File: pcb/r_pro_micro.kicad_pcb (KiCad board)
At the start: 2 copper layers, 31.3 x 32.5 mm, 27 parts, among them J1 Conn_01x12, J2 USB_A, J3 Conn_01x12, U1 MIC5219-2.5YM5, U2 ATmega32U4-MU, Y1 16MHz

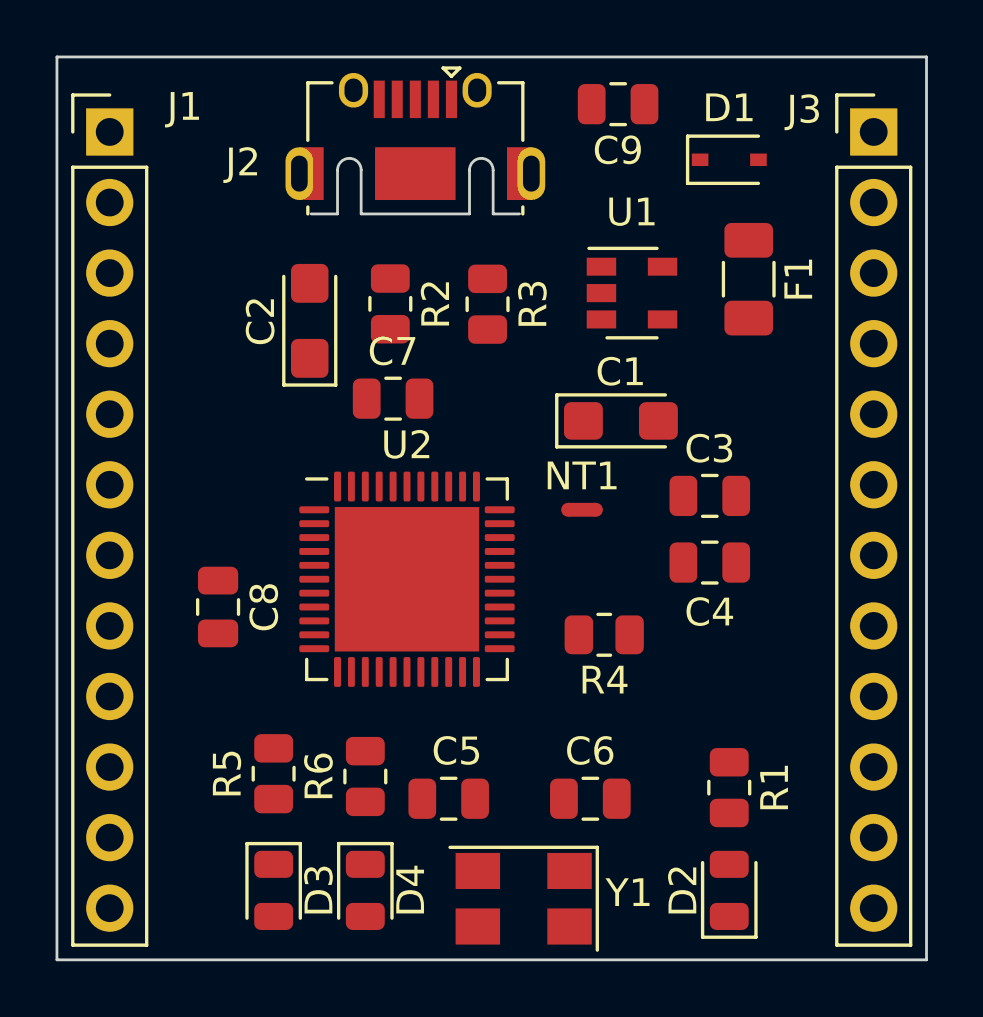
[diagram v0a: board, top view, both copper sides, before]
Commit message: ** Se corrige posicionamiento **
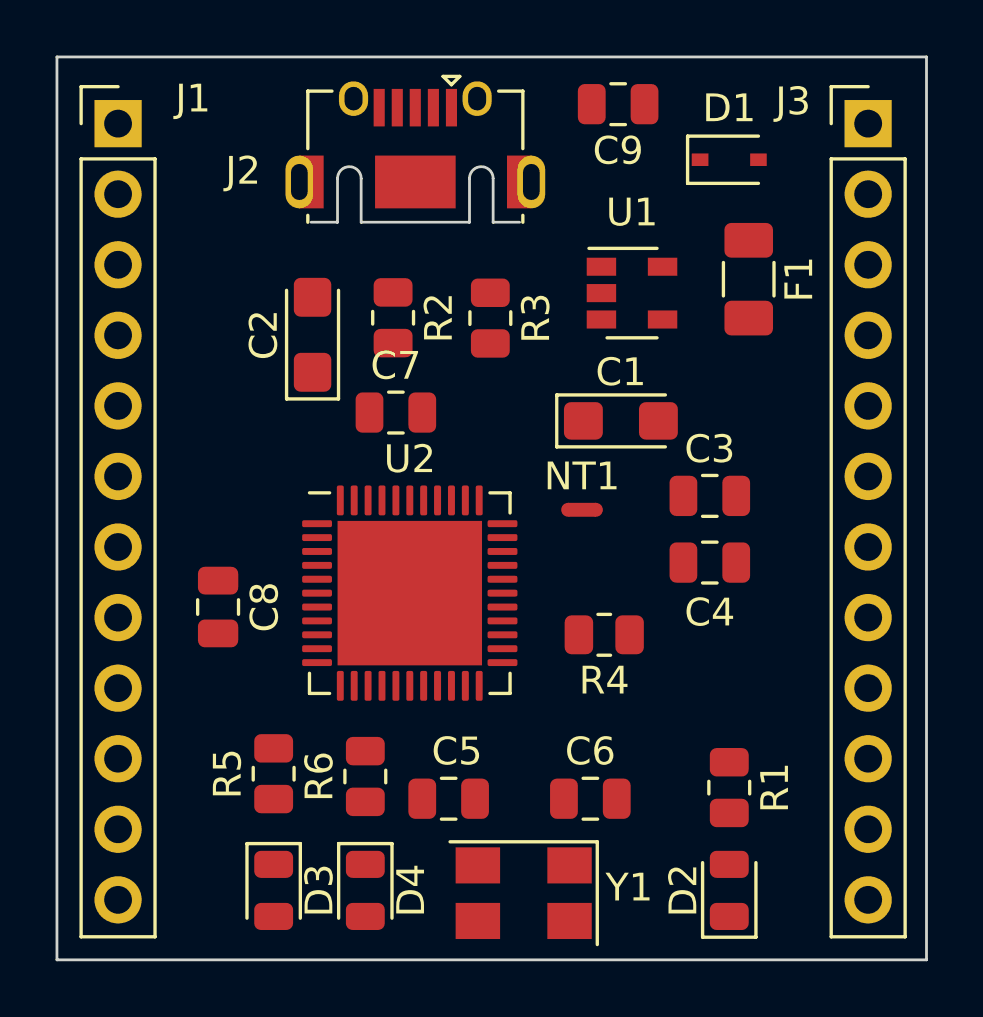
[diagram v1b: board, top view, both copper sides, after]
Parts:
- moved C2 0.51 mm to (145.0, 90.5)
- moved C7 0.51 mm to (148.0, 93.3)
- moved R2 0.51 mm to (147.9, 89.9)
- moved R3 0.51 mm to (151.4, 89.9)
- moved U2 0.51 mm to (148.5, 99.8)
- moved J1 0.42 mm to (138.0, 82.9)
- moved J3 0.36 mm to (165.0, 82.9)
- moved J2 0.30 mm to (148.7, 85.0)
- moved Y1 0.20 mm to (152.6, 110.6)
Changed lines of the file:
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@@
       (effects (font (size 1 1) (thickness 0.15)))
-    )
-    (fp_text user %R (at 0 0) (layer F.Fab)
-      (effects (font (size 0.8 0.8) (thickness 0.12)))
     )
     (fp_line (start 1.6 -0.8) (end -1.2 -0.8) (layer F.Fab) (width 0.1))
@@
     (fp_line (start 2.3 -1.05) (end 2.3 1.05) (layer F.CrtYd) (width 0.05))
     (fp_line (start 2.3 1.05) (end -2.3 1.05) (layer F.CrtYd) (width 0.05))
+    (fp_text user %R (at 0 0) (layer F.Fab)
+      (effects (font (size 0.8 0.8) (thickness 0.12)))
+    )
     (pad 2 smd roundrect (at 1.35 0) (size 1.4 1.35) (layers F.Cu F.Paste F.Mask) (roundrect_rratio 0.185185)
       (net 1 GND))
@@
   )
   (module Capacitor_Tantalum_SMD:CP_EIA-3216-10_Kemet-I (layer F.Cu)
-    (at 144.9 90 90)
+    (at 145 90.5 90)
     (descr "Tantalum Capacitor SMD Kemet-I (3216-10 Metric), IPC_7351 nominal, (Body size from: http://www.kemet.com/Lists/ProductCatalog/Attachments/253/KEM_TC101_STD.pdf), generated with kicad-footprint-generator")
     (tags "capacitor tantalum")
@@
       (effects (font (size 1 1) (thickness 0.15)))
     )
-    (fp_text user %R (at 0 0) (layer F.Fab)
-      (effects (font (size 0.5 0.5) (thickness 0.08)))
-    )
     (fp_line (start -1 0.625) (end -1 -0.625) (layer F.Fab) (width 0.1))
     (fp_line (start -1 -0.625) (end 1 -0.625) (layer F.Fab) (width 0.1))
@@
     (fp_line (start 1.7 -0.98) (end 1.7 0.98) (layer F.CrtYd) (width 0.05))
     (fp_line (start 1.7 0.98) (end -1.7 0.98) (layer F.CrtYd) (width 0.05))
+    (fp_text user %R (at 0 0) (layer F.Fab)
+      (effects (font (size 0.5 0.5) (thickness 0.08)))
+    )
     (pad 2 smd roundrect (at 0.95 0) (size 1 1.45) (layers F.Cu F.Paste F.Mask) (roundrect_rratio 0.25)
       (net 1 GND))
@@
       (effects (font (size 1 1) (thickness 0.15)))
     )
-    (fp_text user %R (at 0 0) (layer F.Fab)
-      (effects (font (size 0.5 0.5) (thickness 0.08)))
-    )
     (fp_line (start -1 0.625) (end -1 -0.625) (layer F.Fab) (width 0.1))
     (fp_line (start -1 -0.625) (end 1 -0.625) (layer F.Fab) (width 0.1))
@@
     (fp_line (start 1.7 -0.98) (end 1.7 0.98) (layer F.CrtYd) (width 0.05))
     (fp_line (start 1.7 0.98) (end -1.7 0.98) (layer F.CrtYd) (width 0.05))
+    (fp_text user %R (at 0 0) (layer F.Fab)
+      (effects (font (size 0.5 0.5) (thickness 0.08)))
+    )
     (pad 2 smd roundrect (at 0.95 0) (size 1 1.45) (layers F.Cu F.Paste F.Mask) (roundrect_rratio 0.25)
       (net 1 GND))
@@
   )
   (module Capacitor_SMD:C_0805_2012Metric (layer F.Cu)
-    (at 147.9 92.8)
+    (at 148 93.3)
     (descr "Capacitor SMD 0805 (2012 Metric), square (rectangular) end terminal, IPC_7351 nominal, (Body size source: IPC-SM-782 page 76, https://www.pcb-3d.com/wordpress/wp-content/uploads/ipc-sm-782a_amendment_1_and_2.pdf, https://docs.google.com/spreadsheets/d/1BsfQQcO9C6DZCsRaXUlFlo91Tg2WpOkGARC1WS5S8t0/edit?usp=sharing), generated with kicad-footprint-generator")
     (tags capacitor)
@@
       (effects (font (size 1 1) (thickness 0.15)))
     )
-    (fp_text user %R (at 0 0 90) (layer F.Fab)
-      (effects (font (size 0.5 0.5) (thickness 0.08)))
-    )
     (fp_line (start -1 0.625) (end -1 -0.625) (layer F.Fab) (width 0.1))
     (fp_line (start -1 -0.625) (end 1 -0.625) (layer F.Fab) (width 0.1))
@@
     (fp_line (start 1.7 -0.98) (end 1.7 0.98) (layer F.CrtYd) (width 0.05))
     (fp_line (start 1.7 0.98) (end -1.7 0.98) (layer F.CrtYd) (width 0.05))
+    (fp_text user %R (at 0 0 90) (layer F.Fab)
+      (effects (font (size 0.5 0.5) (thickness 0.08)))
+    )
     (pad 2 smd roundrect (at 0.95 0 270) (size 1 1.45) (layers F.Cu F.Paste F.Mask) (roundrect_rratio 0.25)
       (net 1 GND))
@@
       (effects (font (size 1 1) (thickness 0.15)))
     )
-    (fp_text user %R (at 0 0 90) (layer F.Fab)
-      (effects (font (size 0.5 0.5) (thickness 0.08)))
-    )
     (fp_line (start 1 -0.6) (end -0.7 -0.6) (layer F.Fab) (width 0.1))
     (fp_line (start -0.7 -0.6) (end -1 -0.3) (layer F.Fab) (width 0.1))
@@
     (fp_line (start 1.68 -0.95) (end 1.68 0.95) (layer F.CrtYd) (width 0.05))
     (fp_line (start 1.68 0.95) (end -1.68 0.95) (layer F.CrtYd) (width 0.05))
+    (fp_text user %R (at 0 0 90) (layer F.Fab)
+      (effects (font (size 0.5 0.5) (thickness 0.08)))
+    )
     (pad 2 smd roundrect (at 0.9375 0 270) (size 0.975 1.4) (layers F.Cu F.Paste F.Mask) (roundrect_rratio 0.25)
       (net 3 +3V3))
@@
   )
   (module Connector_PinHeader_2.54mm:PinHeader_1x12_P2.54mm_Vertical (layer F.Cu)
-    (at 137.7 83.2)
+    (at 138 82.9)
     (descr "Through hole straight pin header, 1x12, 2.54mm pitch, single row")
     (tags "Through hole pin header THT 1x12 2.54mm single row")
@@
     )
     (fp_text value Conn_01x12 (at 0 30.27) (layer F.Fab)
-      (effects (font (size 1 1) (thickness 0.15)))
-    )
-    (fp_text user %R (at 0 13.97 90) (layer F.Fab)
       (effects (font (size 1 1) (thickness 0.15)))
     )
@@
     (fp_line (start 1.8 29.75) (end 1.8 -1.8) (layer F.CrtYd) (width 0.05))
     (fp_line (start 1.8 -1.8) (end -1.8 -1.8) (layer F.CrtYd) (width 0.05))
+    (fp_text user %R (at 0 13.97 90) (layer F.Fab)
+      (effects (font (size 1 1) (thickness 0.15)))
+    )
     (pad 12 thru_hole oval (at 0 27.94) (size 1.7 1.7) (drill 1) (layers *.Cu *.Mask)
       (net 13 /TXO))
@@
   )
   (module Connector_USB:USB_Micro-AB_Molex_47590-0001 (layer F.Cu)
-    (at 148.7 84.7)
+    (at 148.7 85)
     (descr "Micro USB AB receptable, right-angle inverted (https://www.molex.com/pdm_docs/sd/475900001_sd.pdf)")
     (tags "Micro AB USB SMD")
@@
   )
   (module Connector_PinHeader_2.54mm:PinHeader_1x12_P2.54mm_Vertical (layer F.Cu)
-    (at 165.2 83.2)
+    (at 165 82.9)
     (descr "Through hole straight pin header, 1x12, 2.54mm pitch, single row")
     (tags "Through hole pin header THT 1x12 2.54mm single row")
-    (fp_text reference J3 (at -2.5 -0.8) (layer F.SilkS)
+    (fp_text reference J3 (at -2.7 -0.8) (layer F.SilkS)
       (effects (font (size 1 1) (thickness 0.15)))
     )
@@
   )
   (module Resistor_SMD:R_0805_2012Metric (layer F.Cu)
-    (at 147.8 89.3875 270)
+    (at 147.9 89.8875 270)
     (descr "Resistor SMD 0805 (2012 Metric), square (rectangular) end terminal, IPC_7351 nominal, (Body size source: IPC-SM-782 page 72, https://www.pcb-3d.com/wordpress/wp-content/uploads/ipc-sm-782a_amendment_1_and_2.pdf), generated with kicad-footprint-generator")
     (tags resistor)
@@
     (fp_text value 22 (at 0 1.65 90) (layer F.Fab)
       (effects (font (size 1 1) (thickness 0.15)))
-    )
-    (fp_text user %R (at 0 0 90) (layer F.Fab)
-      (effects (font (size 0.5 0.5) (thickness 0.08)))
     )
     (fp_line (start -1 0.625) (end -1 -0.625) (layer F.Fab) (width 0.1))
@@
     (fp_line (start 1.68 -0.95) (end 1.68 0.95) (layer F.CrtYd) (width 0.05))
     (fp_line (start 1.68 0.95) (end -1.68 0.95) (layer F.CrtYd) (width 0.05))
+    (fp_text user %R (at 0 0 90) (layer F.Fab)
+      (effects (font (size 0.5 0.5) (thickness 0.08)))
+    )
     (pad 2 smd roundrect (at 0.9125 0 270) (size 1.025 1.4) (layers F.Cu F.Paste F.Mask) (roundrect_rratio 0.243902)
       (net 24 "Net-(J2-Pad3)"))
@@
   )
   (module Resistor_SMD:R_0805_2012Metric (layer F.Cu)
-    (at 151.3 89.4 270)
+    (at 151.4 89.9 270)
     (descr "Resistor SMD 0805 (2012 Metric), square (rectangular) end terminal, IPC_7351 nominal, (Body size source: IPC-SM-782 page 72, https://www.pcb-3d.com/wordpress/wp-content/uploads/ipc-sm-782a_amendment_1_and_2.pdf), generated with kicad-footprint-generator")
     (tags resistor)
@@
       (effects (font (size 1 1) (thickness 0.15)))
     )
-    (fp_text user %R (at 0 0) (layer F.Fab)
-      (effects (font (size 0.5 0.5) (thickness 0.08)))
-    )
     (fp_line (start -1 0.625) (end -1 -0.625) (layer F.Fab) (width 0.1))
     (fp_line (start -1 -0.625) (end 1 -0.625) (layer F.Fab) (width 0.1))
@@
     (fp_line (start 1.68 -0.95) (end 1.68 0.95) (layer F.CrtYd) (width 0.05))
     (fp_line (start 1.68 0.95) (end -1.68 0.95) (layer F.CrtYd) (width 0.05))
+    (fp_text user %R (at 0 0) (layer F.Fab)
+      (effects (font (size 0.5 0.5) (thickness 0.08)))
+    )
     (pad 2 smd roundrect (at 0.9125 0 180) (size 1.025 1.4) (layers F.Cu F.Paste F.Mask) (roundrect_rratio 0.243902)
       (net 26 /RESET))
@@
       (effects (font (size 1 1) (thickness 0.15)))
     )
-    (fp_text user %R (at 0 0 90) (layer F.Fab)
-      (effects (font (size 0.5 0.5) (thickness 0.08)))
-    )
     (fp_line (start -1 0.625) (end -1 -0.625) (layer F.Fab) (width 0.1))
     (fp_line (start -1 -0.625) (end 1 -0.625) (layer F.Fab) (width 0.1))
@@
     (fp_line (start 1.68 -0.95) (end 1.68 0.95) (layer F.CrtYd) (width 0.05))
     (fp_line (start 1.68 0.95) (end -1.68 0.95) (layer F.CrtYd) (width 0.05))
+    (fp_text user %R (at 0 0 90) (layer F.Fab)
+      (effects (font (size 0.5 0.5) (thickness 0.08)))
+    )
     (pad 2 smd roundrect (at 0.9125 0 90) (size 1.025 1.4) (layers F.Cu F.Paste F.Mask) (roundrect_rratio 0.243902)
       (net 39 "Net-(R6-Pad2)"))
@@
   )
   (module Package_DFN_QFN:QFN-44-1EP_7x7mm_P0.5mm_EP5.2x5.2mm (layer F.Cu)
-    (at 148.4 99.3)
+    (at 148.5 99.8)
     (descr "QFN, 44 Pin (http://ww1.microchip.com/downloads/en/DeviceDoc/2512S.pdf#page=17), generated with kicad-footprint-generator ipc_noLead_generator.py")
     (tags "QFN NoLead")
@@
   )
   (module Crystal:Crystal_SMD_5032-4Pin_5.0x3.2mm (layer F.Cu)
-    (at 152.6 110.8 180)
+    (at 152.6 110.6 180)
     (descr "SMD Crystal SERIES SMD2520/4 http://www.icbase.com/File/PDF/HKC/HKC00061008.pdf, 5.0x3.2mm^2 package")
     (tags "SMD SMT crystal")

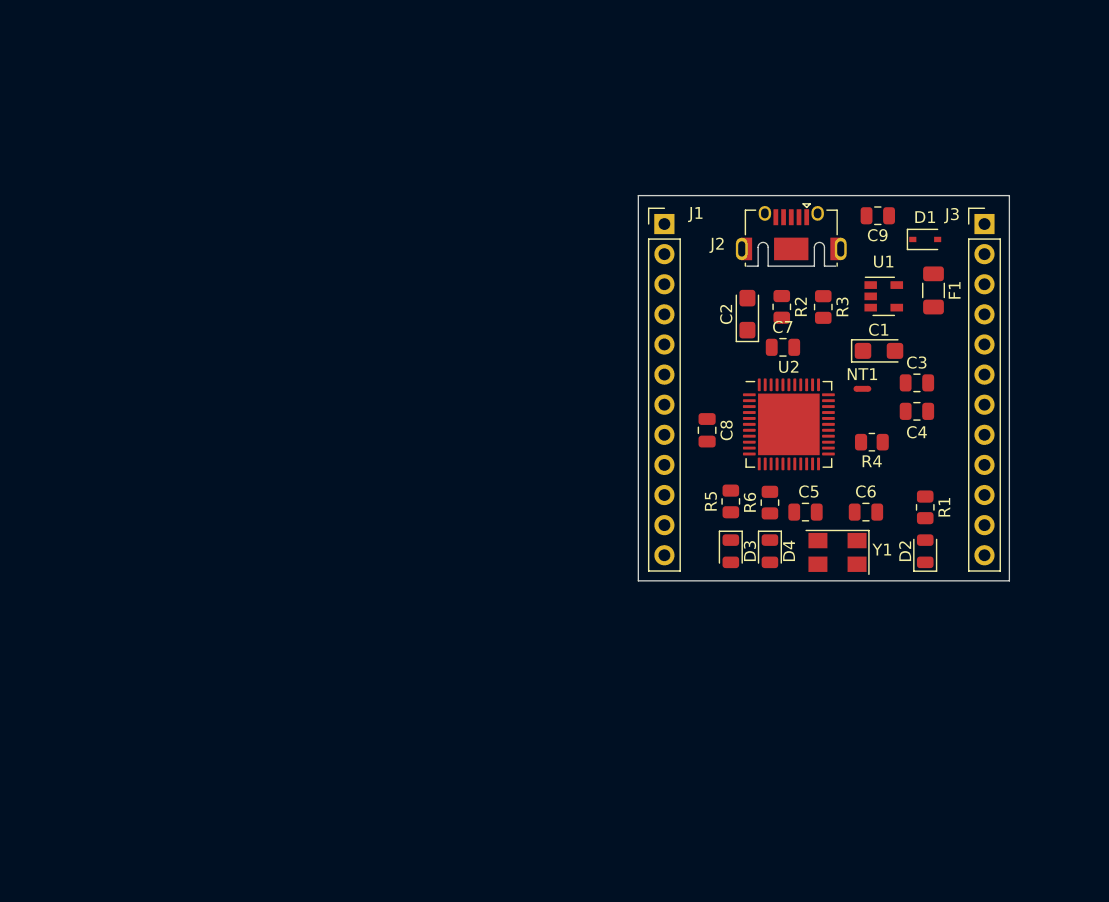
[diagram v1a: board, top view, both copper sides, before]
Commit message: ** Se rehace posicionamiento de footprints **
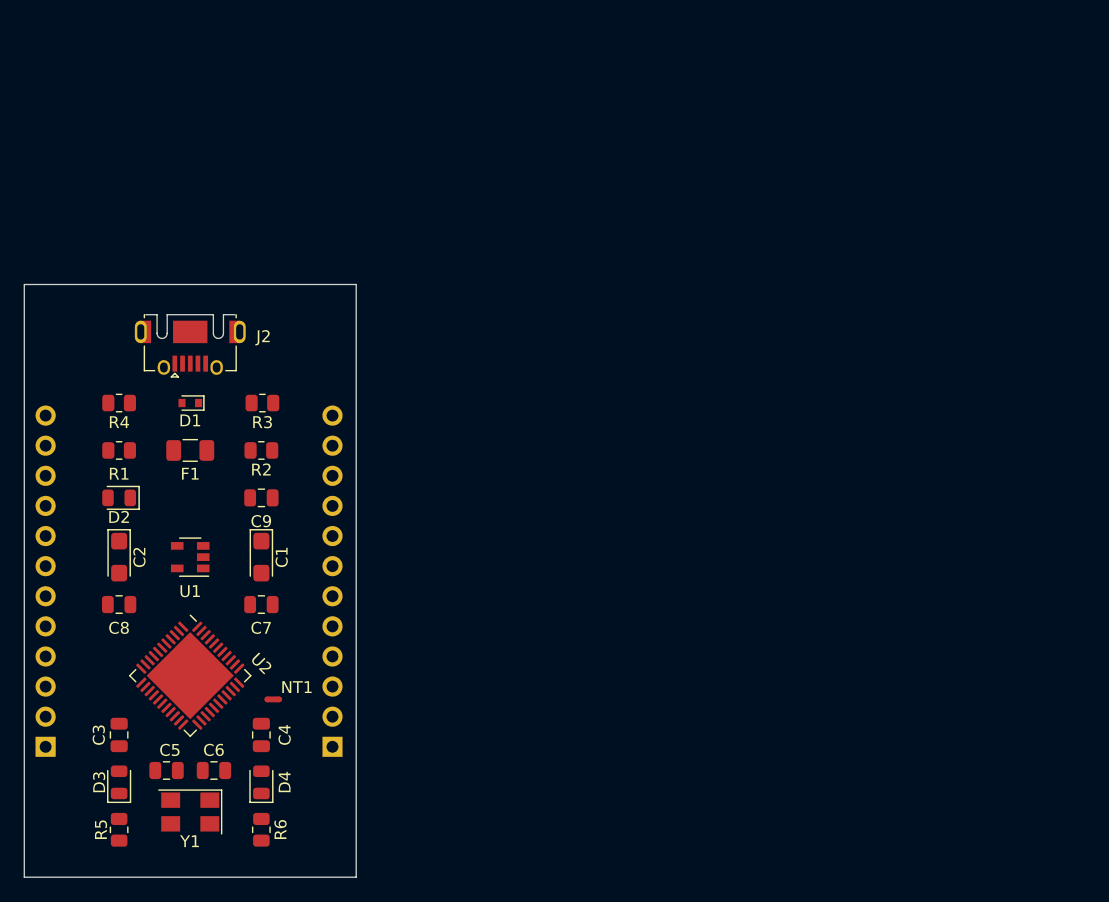
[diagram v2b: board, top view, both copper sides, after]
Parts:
- D1: footprint Diode_SMD:D_SOD-323 -> Diode_SMD:D_SOD-523
- J1, J3: moved to B.Cu
- moved C3 73.6 mm to (92.0, 126.0), turned to 90 degrees
- moved J3 70.5 mm to (110.0, 127.0)
- moved J1 68.3 mm to (85.8, 127.0)
- moved R1 68.2 mm to (92.0, 102.0), turned to 180 degrees
- moved D2 68.1 mm to (92.0, 106.0), turned to 180 degrees
- moved F1 64.1 mm to (98.0, 102.0), turned to 0 degrees
- moved R4 63.6 mm to (92.0, 98.0)
- moved D1 63.5 mm to (98.0, 98.0), turned to 180 degrees
- moved U1 62.5 mm to (98.0, 111.0), turned to 180 degrees
- moved C4 61.7 mm to (104.0, 126.0), turned to 270 degrees
- moved C6 59.2 mm to (100.0, 129.0)
- moved Y1 58.8 mm to (98.0, 132.5)
- moved R5 58.6 mm to (92.0, 134.0), turned to 270 degrees
- moved C5 58.1 mm to (96.0, 129.0)
- moved C9 57.2 mm to (104.0, 106.0), turned to 0 degrees
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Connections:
- J3 pad 1: /RAW -> /D10
- J3 pad 10: /MISO -> /RESET
- J3 pad 11: /MOSI -> GND
- J3 pad 12: /D10 -> /RAW
- J3 pad 2: GND -> /MOSI
- J3 pad 3: /RESET -> /MISO
- J3 pad 4: +3V3 -> /SCK
- J3 pad 5: /A3 -> /A0
- J3 pad 6: /A2 -> /A1
- J3 pad 7: /A1 -> /A2
- J3 pad 8: /A0 -> /A3
- J3 pad 9: /SCK -> +3V3
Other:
- board size 31.3 x 32.5 mm -> 28 x 50 mm
